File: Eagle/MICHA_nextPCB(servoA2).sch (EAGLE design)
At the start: 70 parts, among them IC1 LM4041A12LP, K1 PIN20X2, T1 BSS84, U1 ARDUINO_MKR_ZERO, U2 MIKROE_CLICK_UPGRADE, U3 MAX4528CSA, X1 SS-7188S-A-NF_V2, X2 SS-7188S-A-NF_V2, X3 SS-7188S-A-NF_V2, X4 SS-7188S-A-NF_V2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

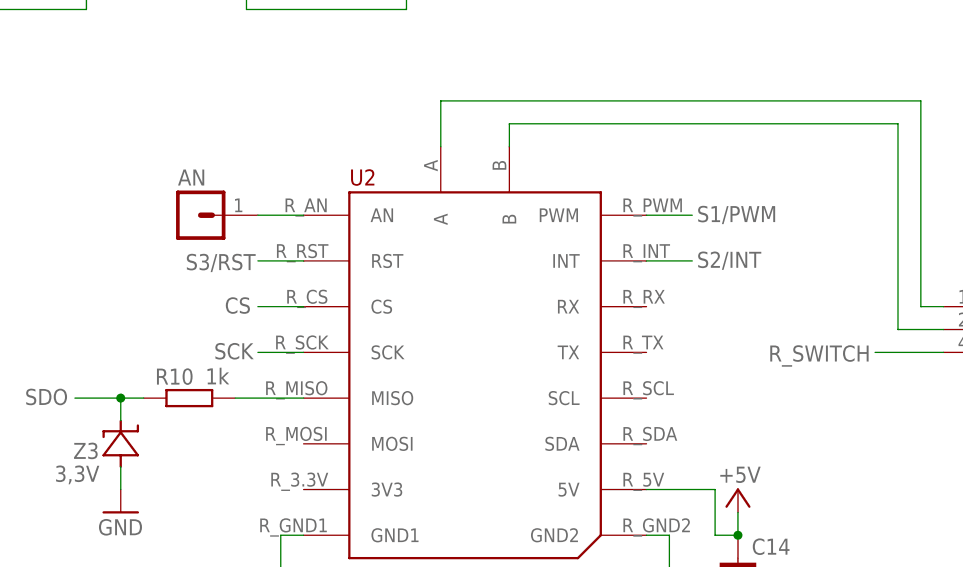
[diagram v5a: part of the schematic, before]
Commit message: Mikrobus footprint updated
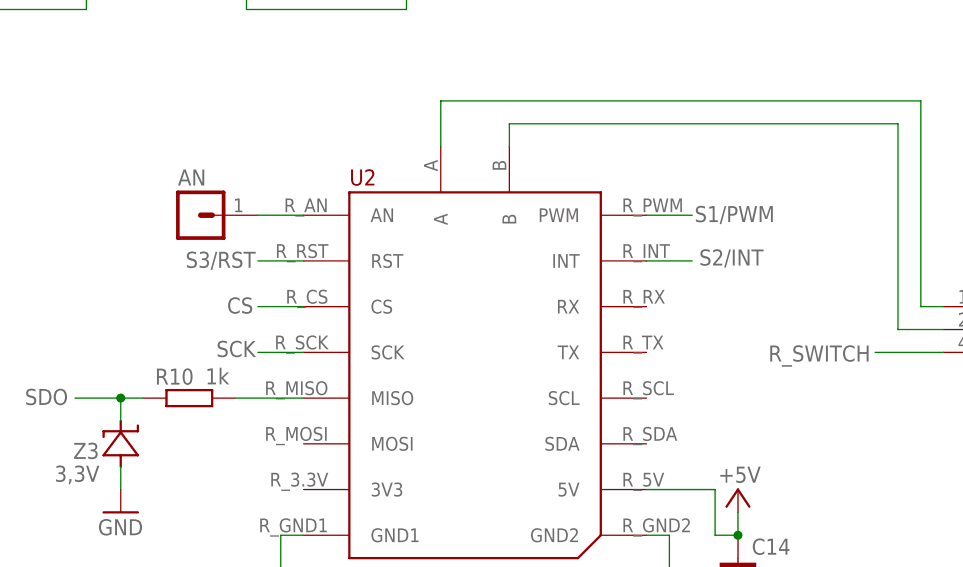
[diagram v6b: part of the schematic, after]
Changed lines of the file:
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@@
 <setting verticaltext="up"/>
 </settings>
-<grid distance="0.1" unitdist="inch" unit="inch" style="lines" multiple="1" display="yes" altdistance="0.01" altunitdist="inch" altunit="inch"/>
+<grid distance="0.1" unitdist="inch" unit="inch" style="lines" multiple="1" display="no" altdistance="0.01" altunitdist="inch" altunit="inch"/>
 <layers>
 <layer number="1" name="Top" color="4" fill="1" visible="no" active="no"/>
@@
 </segment>
 <segment>
-<pinref part="U2" gate="G$1" pin="GND2"/>
-<wire x1="91.44" y1="33.02" x2="93.98" y2="33.02" width="0.1524" layer="91"/>
-<pinref part="GND35" gate="1" pin="GND"/>
-<wire x1="93.98" y1="33.02" x2="93.98" y2="25.4" width="0.1524" layer="91"/>
-</segment>
-<segment>
-<pinref part="U2" gate="G$1" pin="GND1"/>
-<wire x1="53.34" y1="33.02" x2="50.8" y2="33.02" width="0.1524" layer="91"/>
-<pinref part="GND36" gate="1" pin="GND"/>
-<wire x1="50.8" y1="33.02" x2="50.8" y2="25.4" width="0.1524" layer="91"/>
-</segment>
-<segment>
 <pinref part="Z3" gate="G$1" pin="A"/>
 <pinref part="GND11" gate="1" pin="GND"/>
@@
 <wire x1="252.73" y1="124.46" x2="246.38" y2="124.46" width="0.1524" layer="91"/>
 </segment>
+<segment>
+<pinref part="U2" gate="G$1" pin="GND1"/>
+<wire x1="53.34" y1="33.02" x2="50.8" y2="33.02" width="0.1524" layer="91"/>
+<pinref part="GND36" gate="1" pin="GND"/>
+<wire x1="50.8" y1="33.02" x2="50.8" y2="25.4" width="0.1524" layer="91"/>
+</segment>
+<segment>
+<pinref part="U2" gate="G$1" pin="GND2"/>
+<wire x1="91.44" y1="33.02" x2="93.98" y2="33.02" width="0.1524" layer="91"/>
+<pinref part="GND35" gate="1" pin="GND"/>
+<wire x1="93.98" y1="33.02" x2="93.98" y2="25.4" width="0.1524" layer="91"/>
+</segment>
 </net>
 <net name="+5V" class="0">
@@
 </segment>
 <segment>
-<pinref part="U2" gate="G$1" pin="5V"/>
-<wire x1="91.44" y1="38.1" x2="99.06" y2="38.1" width="0.1524" layer="91"/>
 <wire x1="99.06" y1="38.1" x2="99.06" y2="33.02" width="0.1524" layer="91"/>
 <pinref part="C14" gate="G$1" pin="1"/>
@@
 <wire x1="101.6" y1="35.56" x2="101.6" y2="33.02" width="0.1524" layer="91"/>
 <junction x="101.6" y="33.02"/>
+<pinref part="U2" gate="G$1" pin="5V"/>
+<wire x1="91.44" y1="38.1" x2="99.06" y2="38.1" width="0.1524" layer="91"/>
 </segment>
 </net>
@@
 <pinref part="U2" gate="G$1" pin="CS"/>
 <wire x1="53.34" y1="58.42" x2="48.26" y2="58.42" width="0.1524" layer="91"/>
-<label x="47.498" y="59.436" size="1.778" layer="95" rot="R180"/>
+<label x="47.752" y="59.436" size="1.778" layer="95" rot="R180"/>
 </segment>
 </net>
@@
 <pinref part="U2" gate="G$1" pin="SCK"/>
 <wire x1="53.34" y1="53.34" x2="48.26" y2="53.34" width="0.1524" layer="91"/>
-<label x="47.752" y="54.356" size="1.778" layer="95" rot="R180"/>
+<label x="48.006" y="54.61" size="1.778" layer="95" rot="R180"/>
 </segment>
 </net>
@@
 <pinref part="U2" gate="G$1" pin="PWM"/>
 <wire x1="91.44" y1="68.58" x2="96.52" y2="68.58" width="0.1524" layer="91"/>
-<label x="97.028" y="67.818" size="1.778" layer="95"/>
+<label x="96.774" y="67.818" size="1.778" layer="95"/>
 </segment>
 </net>
@@
 <pinref part="U2" gate="G$1" pin="INT"/>
 <wire x1="91.44" y1="63.5" x2="96.52" y2="63.5" width="0.1524" layer="91"/>
-<label x="97.028" y="62.738" size="1.778" layer="95"/>
+<label x="97.282" y="62.992" size="1.778" layer="95"/>
 </segment>
 </net>
@@
 <pinref part="U2" gate="G$1" pin="RST"/>
 <wire x1="53.34" y1="63.5" x2="48.26" y2="63.5" width="0.1524" layer="91"/>
-<label x="48.006" y="64.262" size="1.778" layer="95" rot="R180"/>
+<label x="48.006" y="64.516" size="1.778" layer="95" rot="R180"/>
 </segment>
 </net>
@@
 <net name="N$1" class="0">
 <segment>
-<pinref part="U2" gate="G$1" pin="B"/>
-<wire x1="76.2" y1="76.2" x2="76.2" y2="78.74" width="0.1524" layer="91"/>
 <wire x1="76.2" y1="78.74" x2="119.38" y2="78.74" width="0.1524" layer="91"/>
 <wire x1="119.38" y1="78.74" x2="119.38" y2="55.88" width="0.1524" layer="91"/>
 <pinref part="U3" gate="A" pin="B"/>
 <wire x1="119.38" y1="55.88" x2="124.46" y2="55.88" width="0.1524" layer="91"/>
+<pinref part="U2" gate="G$1" pin="B"/>
+<wire x1="76.2" y1="76.2" x2="76.2" y2="78.74" width="0.1524" layer="91"/>
 </segment>
 </net>
 <net name="N$10" class="0">
 <segment>
-<pinref part="U2" gate="G$1" pin="A"/>
-<wire x1="68.58" y1="76.2" x2="68.58" y2="81.28" width="0.1524" layer="91"/>
 <wire x1="68.58" y1="81.28" x2="121.92" y2="81.28" width="0.1524" layer="91"/>
 <pinref part="U3" gate="A" pin="A"/>
 <wire x1="121.92" y1="81.28" x2="121.92" y2="58.42" width="0.1524" layer="91"/>
 <wire x1="121.92" y1="58.42" x2="124.46" y2="58.42" width="0.1524" layer="91"/>
+<pinref part="U2" gate="G$1" pin="A"/>
+<wire x1="68.58" y1="76.2" x2="68.58" y2="81.28" width="0.1524" layer="91"/>
 </segment>
 </net>
@@
 </segment>
 </net>
-<net name="N$15" class="0">
-<segment>
-<pinref part="U2" gate="G$1" pin="MISO"/>
-<pinref part="R10" gate="G$1" pin="2"/>
-<wire x1="53.34" y1="48.26" x2="45.72" y2="48.26" width="0.1524" layer="91"/>
-</segment>
-</net>
-<net name="N$16" class="0">
-<segment>
-<pinref part="U2" gate="G$1" pin="AN"/>
-<pinref part="AN" gate="G$1" pin="1"/>
-<wire x1="53.34" y1="68.58" x2="48.26" y2="68.58" width="0.1524" layer="91"/>
-</segment>
-</net>
 <net name="N$17" class="0">
 <segment>
@@
 </segment>
 </net>
+<net name="N$16" class="0">
+<segment>
+<pinref part="U2" gate="G$1" pin="AN"/>
+<pinref part="AN" gate="G$1" pin="1"/>
+<wire x1="53.34" y1="68.58" x2="48.26" y2="68.58" width="0.1524" layer="91"/>
+</segment>
+</net>
+<net name="N$15" class="0">
+<segment>
+<pinref part="U2" gate="G$1" pin="MISO"/>
+<pinref part="R10" gate="G$1" pin="2"/>
+<wire x1="53.34" y1="48.26" x2="45.72" y2="48.26" width="0.1524" layer="91"/>
+</segment>
+</net>
